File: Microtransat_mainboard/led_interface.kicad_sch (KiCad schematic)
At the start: 10 parts, among them J6 Conn_01x05

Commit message: add estop stuff kinda
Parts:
- removed J6: Conn_01x05, symbol Connector_Generic:Conn_01x05
- added J3: Conn_01x06, symbol Connector_Generic:Conn_01x06
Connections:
- net GND: now also J3.6 (Pin_6)
- net blueOut: now also J3.4 (Pin_4)
- net greenOut: now also J3.3 (Pin_3)
- net redOut: now also J3.1 (Pin_1)
- net yellowOut: now also J3.2 (Pin_2)
- net eStopOut: now reaches Logic_Shifter1.11 (B5)
- net eStopOut: now also J3.5 (Pin_5)
- net eStopTrigger: now reaches Logic_Shifter1.6 (A5)
- no-connect marks 4 -> 2
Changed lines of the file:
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@@
-	)
-	(no_connect
-		(at 165.1 87.63)
 	)
 	(no_connect
@@
 	)
 	(no_connect
-		(at 165.1 77.47)
-	)
-	(no_connect
 		(at 165.1 80.01)
 	)
@@
 			)
 			(justify right bottom)
+		)
+	)
+	(label "eStopOut"
+		(at 194.31 88.9 180)
+		(effects
+			(font
+				(size 1.27 1.27)
+			)
+			(justify right bottom)
+		)
+	)
+	(label "eStopOut"
+		(at 165.1 87.63 0)
+		(effects
+			(font
+				(size 1.27 1.27)
+			)
+			(justify left bottom)
 		)
 	)
@@
 			)
 			(justify right)
+		)
+	)
+	(hierarchical_label "eStopTrigger"
+		(shape input)
+		(at 165.1 77.47 0)
+		(effects
+			(font
+				(size 1.27 1.27)
+			)
+			(justify left)
 		)
 	)
@@
 	)
 	(symbol
-		(lib_id "Connector_Generic:Conn_01x05")
-		(at 199.39 83.82 0)
-		(unit 1)
-		(exclude_from_sim no)
-		(in_bom yes)
-		(on_board yes)
-		(dnp no)
-		(fields_autoplaced yes)
-		(property "Reference" "J6"
-			(at 201.93 82.5499 0)
-			(effects
-				(font
-					(size 1.27 1.27)
-				)
-				(justify left)
-			)
-		)
-		(property "Value" "Conn_01x05"
-			(at 201.93 85.0899 0)
-			(effects
-				(font
-					(size 1.27 1.27)
-				)
-				(justify left)
-			)
-		)
-		(property "Footprint" ""
-			(at 199.39 83.82 0)
-			(effects
-				(font
-					(size 1.27 1.27)
-				)
-				(hide yes)
-			)
-		)
-		(property "Datasheet" "~"
-			(at 199.39 83.82 0)
-			(effects
-				(font
-					(size 1.27 1.27)
-				)
-				(hide yes)
-			)
-		)
-		(property "Description" "Generic connector, single row, 01x05, script generated (kicad-library-utils/schlib/autogen/connector/)"
-			(at 199.39 83.82 0)
-			(effects
-				(font
-					(size 1.27 1.27)
-				)
-				(hide yes)
-			)
-		)
-		(pin "1"
-		)
-		(pin "2"
-		)
-		(pin "3"
-		)
-		(pin "5"
-		)
-		(pin "4"
-		)
-		(instances
-			(project "Microtransat_mainboard"
-				(path "/89914625-be83-416e-bb0d-b792f59b4aa6/2a723dab-0fe3-42a5-a32e-d625b3338ba9"
-					(reference "J6")
-					(unit 1)
-				)
-			)
-		)
-	)
-	(symbol
 		(lib_id "Device:LED")
 		(at 68.58 71.12 90)
@@
 	(symbol
 		(lib_id "power:GND")
-		(at 194.31 88.9 270)
+		(at 194.31 91.44 270)
 		(unit 1)
 		(exclude_from_sim no)
@@
 		(dnp no)
 		(property "Reference" "#PWR041"
-			(at 187.96 88.9 0)
+			(at 187.96 91.44 0)
 			(effects
 				(font
@@
 		)
 		(property "Value" "GND"
-			(at 189.23 88.9 90)
+			(at 189.23 91.44 90)
 			(effects
 				(font
@@
 		)
 		(property "Footprint" ""
-			(at 194.31 88.9 0)
+			(at 194.31 91.44 0)
 			(effects
 				(font
@@
 		)
 		(property "Datasheet" ""
-			(at 194.31 88.9 0)
+			(at 194.31 91.44 0)
 			(effects
 				(font
@@
 		)
 		(property "Description" "Power symbol creates a global label with name \"GND\" , ground"
-			(at 194.31 88.9 0)
+			(at 194.31 91.44 0)
 			(effects
 				(font
@@
 					(unit 1)
 				)
+			)
+		)
+	)
+	(symbol
+		(lib_id "Connector_Generic:Conn_01x06")
+		(at 199.39 83.82 0)
+		(unit 1)
+		(exclude_from_sim no)
+		(in_bom yes)
+		(on_board yes)
+		(dnp no)
+		(fields_autoplaced yes)
+		(property "Reference" "J3"
+			(at 201.93 83.8199 0)
+			(effects
+				(font
+					(size 1.27 1.27)
+				)
+				(justify left)
+			)
+		)
+		(property "Value" "Conn_01x06"
+			(at 201.93 86.3599 0)
+			(effects
+				(font
+					(size 1.27 1.27)
+				)
+				(justify left)
+			)
+		)
+		(property "Footprint" ""
+			(at 199.39 83.82 0)
+			(effects
+				(font
+					(size 1.27 1.27)
+				)
+				(hide yes)
+			)
+		)
+		(property "Datasheet" "~"
+			(at 199.39 83.82 0)
+			(effects
+				(font
+					(size 1.27 1.27)
+				)
+				(hide yes)
+			)
+		)
+		(property "Description" "Generic connector, single row, 01x06, script generated (kicad-library-utils/schlib/autogen/connector/)"
+			(at 199.39 83.82 0)
+			(effects
+				(font
+					(size 1.27 1.27)
+				)
+				(hide yes)
+			)
+		)
+		(pin "4"
+		)
+		(pin "1"
+		)
+		(pin "5"
+		)
+		(pin "3"
+		)
+		(pin "6"
+		)
+		(pin "2"
+		)
+		(instances
+			(project ""
+				(path "/89914625-be83-416e-bb0d-b792f59b4aa6/2a723dab-0fe3-42a5-a32e-d625b3338ba9"
+					(reference "J3")
+					(unit 1)
+				)

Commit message: puh
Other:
- note added: "Relay Out"
- note removed: "Light Tower Out"
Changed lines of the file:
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@@
 	(generator_version "9.0")
 	(paper "A4")
-	(text "Light Tower Out\n"
+	(text "Relay Out"
 		(exclude_from_sim no)
 		(at 198.882 74.93 0)

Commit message: Fixed ERC errors
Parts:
- J3: footprint (none) -> Connector_PinHeader_2.54mm:PinHeader_1x06_P2.54mm_Vertical
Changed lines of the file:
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@@
 			)
 		)
-		(property "Footprint" ""
+		(property "Footprint" "Connector_PinHeader_2.54mm:PinHeader_1x06_P2.54mm_Vertical"
 			(at 199.39 83.82 0)
 			(effects

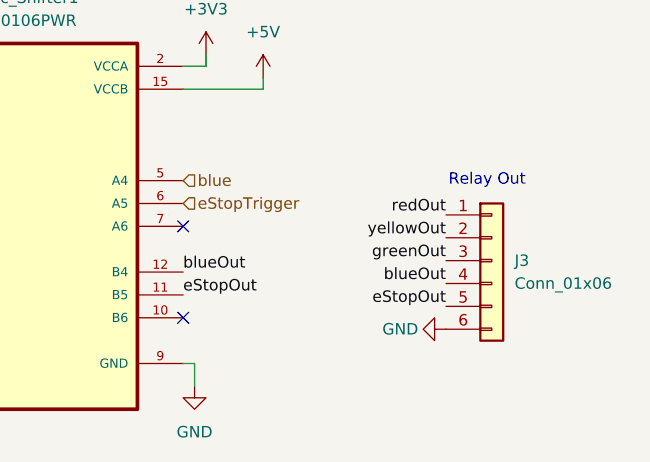
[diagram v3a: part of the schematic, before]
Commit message: Added second RC switch for mode pin, added additional relay output, changed IMU to I2C
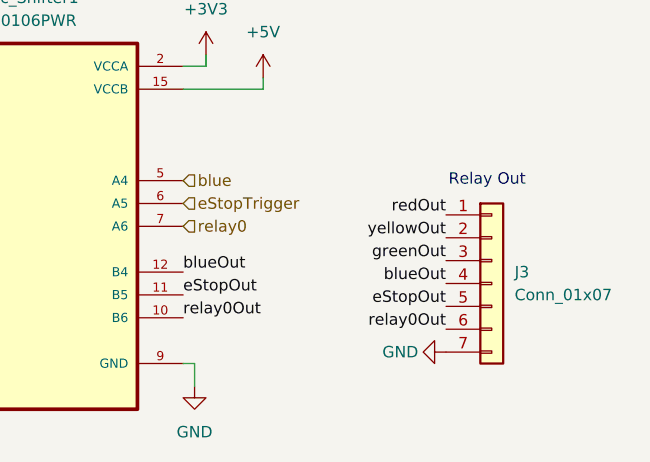
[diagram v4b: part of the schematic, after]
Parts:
- removed J3: Conn_01x06, Connector_PinHeader_2.54mm:PinHeader_1x06_P2.54mm_Vertical, symbol Connector_Generic:Conn_01x06
- added J3: Conn_01x07, Connector_PinSocket_2.54mm:PinSocket_1x07_P2.54mm_Vertical, symbol Connector_Generic:Conn_01x07
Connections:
- net GND: now also J3.7 (Pin_7)
- net blueOut: now also J3.4 (Pin_4)
- net eStopOut: now also J3.5 (Pin_5)
- net greenOut: now also J3.3 (Pin_3)
- net redOut: now also J3.1 (Pin_1)
- net yellowOut: now also J3.2 (Pin_2)
- net relay0Out: now reaches Logic_Shifter1.10 (B6)
- net relay0Out: now also J3.6 (Pin_6)
- net relay0: now reaches Logic_Shifter1.7 (A6)
- no-connect marks 2 -> 0
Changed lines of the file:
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@@
 		(color 0 0 0 0)
-	)
-	(no_connect
-		(at 165.1 90.17)
-	)
-	(no_connect
-		(at 165.1 80.01)
 	)
 	(wire
@@
 		)
 	)
+	(label "relay0Out"
+		(at 194.31 91.44 180)
+		(effects
+			(font
+				(size 1.27 1.27)
+			)
+			(justify right bottom)
+		)
+	)
 	(label "yellowOut"
 		(at 194.31 81.28 180)
@@
 			)
 			(justify right bottom)
+		)
+	)
+	(label "relay0Out"
+		(at 165.1 90.17 0)
+		(effects
+			(font
+				(size 1.27 1.27)
+			)
+			(justify left bottom)
 		)
 	)
@@
 		(shape input)
 		(at 68.58 64.77 90)
+		(effects
+			(font
+				(size 1.27 1.27)
+			)
+			(justify left)
+		)
+	)
+	(hierarchical_label "relay0"
+		(shape input)
+		(at 165.1 80.01 0)
 		(effects
 			(font
@@
 	)
 	(symbol
+		(lib_id "Connector_Generic:Conn_01x07")
+		(at 199.39 86.36 0)
+		(unit 1)
+		(exclude_from_sim no)
+		(in_bom yes)
+		(on_board yes)
+		(dnp no)
+		(fields_autoplaced yes)
+		(property "Reference" "J3"
+			(at 201.93 85.0899 0)
+			(effects
+				(font
+					(size 1.27 1.27)
+				)
+				(justify left)
+			)
+		)
+		(property "Value" "Conn_01x07"
+			(at 201.93 87.6299 0)
+			(effects
+				(font
+					(size 1.27 1.27)
+				)
+				(justify left)
+			)
+		)
+		(property "Footprint" "Connector_PinSocket_2.54mm:PinSocket_1x07_P2.54mm_Vertical"
+			(at 199.39 86.36 0)
+			(effects
+				(font
+					(size 1.27 1.27)
+				)
+				(hide yes)
+			)
+		)
+		(property "Datasheet" "~"
+			(at 199.39 86.36 0)
+			(effects
+				(font
+					(size 1.27 1.27)
+				)
+				(hide yes)
+			)
+		)
+		(property "Description" "Generic connector, single row, 01x07, script generated (kicad-library-utils/schlib/autogen/connector/)"
+			(at 199.39 86.36 0)
+			(effects
+				(font
+					(size 1.27 1.27)
+				)
+				(hide yes)
+			)
+		)
+		(pin "5"
+		)
+		(pin "2"
+		)
+		(pin "1"
+		)
+		(pin "3"
+		)
+		(pin "4"
+		)
+		(pin "6"
+		)
+		(pin "7"
+		)
+		(instances
+			(project ""
+				(path "/89914625-be83-416e-bb0d-b792f59b4aa6/2a723dab-0fe3-42a5-a32e-d625b3338ba9"
+					(reference "J3")
+					(unit 1)
+				)
+			)
+		)
+	)
+	(symbol
 		(lib_id "Device:LED")
 		(at 102.87 71.12 90)
@@
 	(symbol
 		(lib_id "power:GND")
-		(at 194.31 91.44 270)
+		(at 194.31 93.98 270)
 		(unit 1)
 		(exclude_from_sim no)
@@
 		(dnp no)
 		(property "Reference" "#PWR041"
-			(at 187.96 91.44 0)
+			(at 187.96 93.98 0)
 			(effects
 				(font
@@
 		)
 		(property "Value" "GND"
-			(at 189.23 91.44 90)
+			(at 189.23 93.98 90)
 			(effects
 				(font
@@
 		)
 		(property "Footprint" ""
-			(at 194.31 91.44 0)
+			(at 194.31 93.98 0)
 			(effects
 				(font
@@
 		)
 		(property "Datasheet" ""
-			(at 194.31 91.44 0)
+			(at 194.31 93.98 0)
 			(effects
 				(font
@@
 		)
 		(property "Description" "Power symbol creates a global label with name \"GND\" , ground"
-			(at 194.31 91.44 0)
+			(at 194.31 93.98 0)
 			(effects
 				(font
@@
 					(unit 1)
 				)
-			)
-		)
-	)
-	(symbol
-		(lib_id "Connector_Generic:Conn_01x06")
-		(at 199.39 83.82 0)
-		(unit 1)
-		(exclude_from_sim no)
-		(in_bom yes)
-		(on_board yes)
-		(dnp no)
-		(fields_autoplaced yes)
-		(property "Reference" "J3"
-			(at 201.93 83.8199 0)
-			(effects
-				(font
-					(size 1.27 1.27)
-				)
-				(justify left)
-			)
-		)
-		(property "Value" "Conn_01x06"
-			(at 201.93 86.3599 0)
-			(effects
-				(font
-					(size 1.27 1.27)
-				)
-				(justify left)
-			)
-		)
-		(property "Footprint" "Connector_PinHeader_2.54mm:PinHeader_1x06_P2.54mm_Vertical"
-			(at 199.39 83.82 0)
-			(effects
-				(font
-					(size 1.27 1.27)
-				)
-				(hide yes)
-			)
-		)
-		(property "Datasheet" "~"
-			(at 199.39 83.82 0)
-			(effects
-				(font
-					(size 1.27 1.27)
-				)
-				(hide yes)
-			)
-		)
-		(property "Description" "Generic connector, single row, 01x06, script generated (kicad-library-utils/schlib/autogen/connector/)"
-			(at 199.39 83.82 0)
-			(effects
-				(font
-					(size 1.27 1.27)
-				)
-				(hide yes)
-			)
-		)
-		(pin "4"
-		)
-		(pin "1"
-		)
-		(pin "5"
-		)
-		(pin "3"
-		)
-		(pin "6"
-		)
-		(pin "2"
-		)
-		(instances
-			(project ""
-				(path "/89914625-be83-416e-bb0d-b792f59b4aa6/2a723dab-0fe3-42a5-a32e-d625b3338ba9"
-					(reference "J3")
-					(unit 1)
-				)

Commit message: routed the traces (maybe?)
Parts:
- added C2, C3: 0.1u, Capacitor_SMD:C_1206_3216Metric_Pad1.33x1.80mm_HandSolder, symbol Device:C
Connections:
- net +3V3: now also C2.1
- net +5V: now also C3.1
- net GND: now also C2.2, C3.2

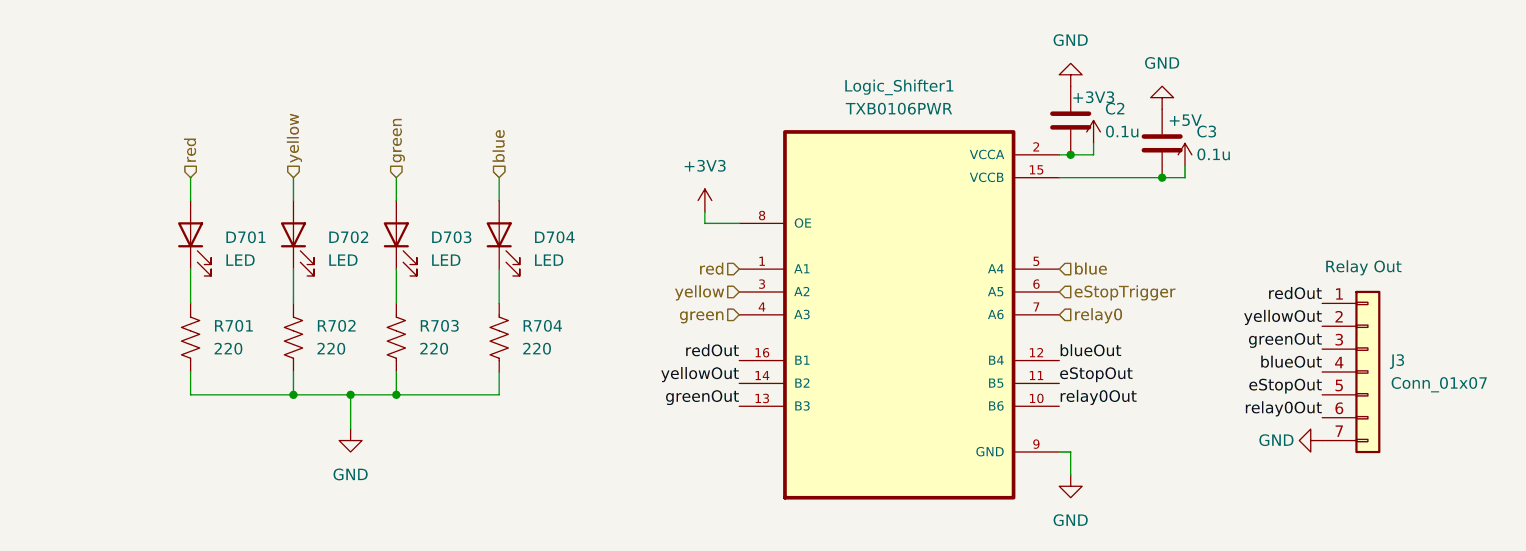
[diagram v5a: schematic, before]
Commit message: Finished silkscreen/outline changes
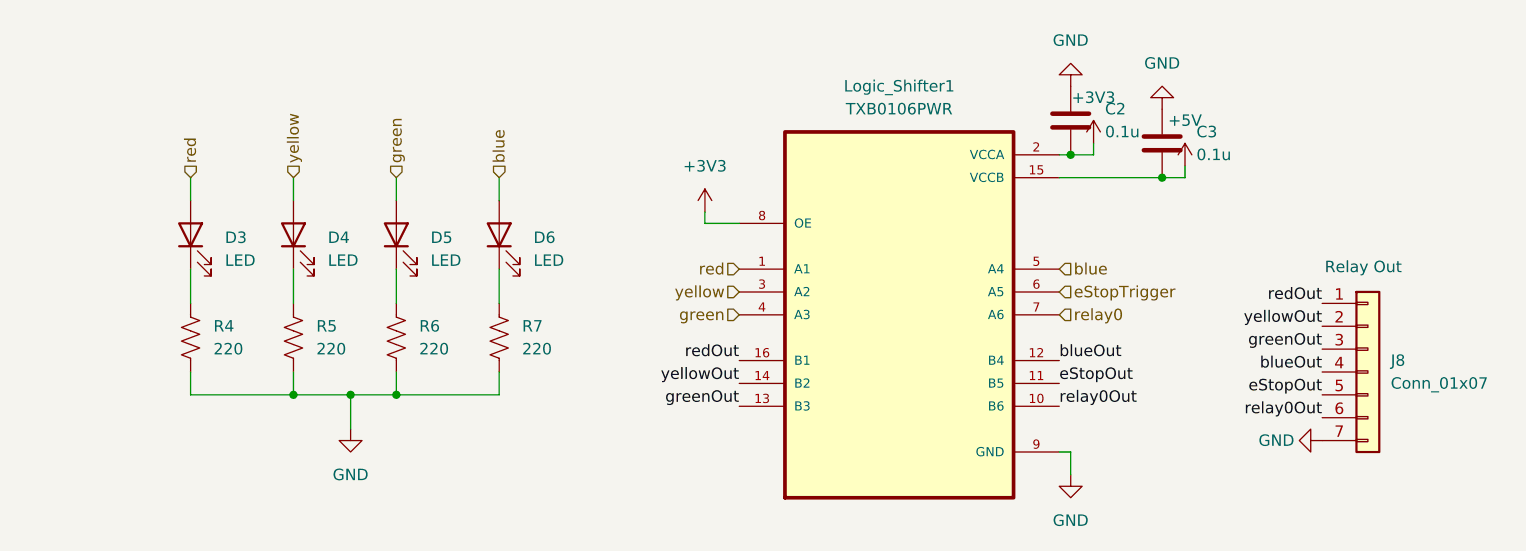
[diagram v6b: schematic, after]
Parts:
- renumbered D701 to D3, D702 to D4, D703 to D5, D704 to D6, J3 to J8, R701 to R4, R702 to R5, R703 to R6, R704 to R7
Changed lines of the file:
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@@
 		(dnp no)
 		(fields_autoplaced yes)
-		(property "Reference" "R703"
+		(property "Reference" "R6"
 			(at 93.98 81.2799 0)
 			(effects
@@
 			(project "Microtransat_mainboard"
 				(path "/89914625-be83-416e-bb0d-b792f59b4aa6/2a723dab-0fe3-42a5-a32e-d625b3338ba9"
-					(reference "R703")
+					(reference "R6")
 					(unit 1)
 				)
@@
 		(dnp no)
 		(fields_autoplaced yes)
-		(property "Reference" "R701"
+		(property "Reference" "R4"
 			(at 71.12 81.2799 0)
 			(effects
@@
 			(project "Microtransat_mainboard"
 				(path "/89914625-be83-416e-bb0d-b792f59b4aa6/2a723dab-0fe3-42a5-a32e-d625b3338ba9"
-					(reference "R701")
+					(reference "R4")
 					(unit 1)
 				)
@@
 		(dnp no)
 		(fields_autoplaced yes)
-		(property "Reference" "#PWR020"
+		(property "Reference" "#PWR031"
 			(at 168.91 64.77 0)
 			(effects
@@
 			(project "Microtransat_mainboard"
 				(path "/89914625-be83-416e-bb0d-b792f59b4aa6/2a723dab-0fe3-42a5-a32e-d625b3338ba9"
-					(reference "#PWR020")
+					(reference "#PWR031")
 					(unit 1)
 				)
@@
 		(dnp no)
 		(fields_autoplaced yes)
-		(property "Reference" "R704"
+		(property "Reference" "R7"
 			(at 105.41 81.2799 0)
 			(effects
@@
 			(project "Microtransat_mainboard"
 				(path "/89914625-be83-416e-bb0d-b792f59b4aa6/2a723dab-0fe3-42a5-a32e-d625b3338ba9"
-					(reference "R704")
+					(reference "R7")
 					(unit 1)
 				)
@@
 		(dnp no)
 		(fields_autoplaced yes)
-		(property "Reference" "D702"
+		(property "Reference" "D4"
 			(at 83.82 71.4374 90)
 			(effects
@@
 			(project "Microtransat_mainboard"
 				(path "/89914625-be83-416e-bb0d-b792f59b4aa6/2a723dab-0fe3-42a5-a32e-d625b3338ba9"
-					(reference "D702")
+					(reference "D4")
 					(unit 1)
 				)
@@
 		(dnp no)
 		(fields_autoplaced yes)
-		(property "Reference" "#PWR021"
+		(property "Reference" "#PWR033"
 			(at 179.07 67.31 0)
 			(effects
@@
 			(project "Microtransat_mainboard"
 				(path "/89914625-be83-416e-bb0d-b792f59b4aa6/2a723dab-0fe3-42a5-a32e-d625b3338ba9"
-					(reference "#PWR021")
+					(reference "#PWR033")
 					(unit 1)
 				)
@@
 		(dnp no)
 		(fields_autoplaced yes)
-		(property "Reference" "J3"
+		(property "Reference" "J8"
 			(at 201.93 85.0899 0)
 			(effects
@@
 			(project ""
 				(path "/89914625-be83-416e-bb0d-b792f59b4aa6/2a723dab-0fe3-42a5-a32e-d625b3338ba9"
-					(reference "J3")
+					(reference "J8")
 					(unit 1)
 				)
@@
 		(dnp no)
 		(fields_autoplaced yes)
-		(property "Reference" "D704"
+		(property "Reference" "D6"
 			(at 106.68 71.4374 90)
 			(effects
@@
 			(project "Microtransat_mainboard"
 				(path "/89914625-be83-416e-bb0d-b792f59b4aa6/2a723dab-0fe3-42a5-a32e-d625b3338ba9"
-					(reference "D704")
+					(reference "D6")
 					(unit 1)
 				)
@@
 		(dnp no)
 		(fields_autoplaced yes)
-		(property "Reference" "#PWR037"
+		(property "Reference" "#PWR029"
 			(at 166.37 48.26 0)
 			(effects
@@
 			(project "Microtransat_mainboard"
 				(path "/89914625-be83-416e-bb0d-b792f59b4aa6/2a723dab-0fe3-42a5-a32e-d625b3338ba9"
-					(reference "#PWR037")
+					(reference "#PWR029")
 					(unit 1)
 				)
@@
 		(dnp no)
 		(fields_autoplaced yes)
-		(property "Reference" "#PWR023"
+		(property "Reference" "#PWR030"
 			(at 166.37 104.14 0)
 			(effects
@@
 			(project "Microtransat_mainboard"
 				(path "/89914625-be83-416e-bb0d-b792f59b4aa6/2a723dab-0fe3-42a5-a32e-d625b3338ba9"
-					(reference "#PWR023")
+					(reference "#PWR030")
 					(unit 1)
 				)
@@
 		(dnp no)
 		(fields_autoplaced yes)
-		(property "Reference" "#PWR039"
+		(property "Reference" "#PWR032"
 			(at 176.53 50.8 0)
 			(effects
@@
 			(project "Microtransat_mainboard"
 				(path "/89914625-be83-416e-bb0d-b792f59b4aa6/2a723dab-0fe3-42a5-a32e-d625b3338ba9"
-					(reference "#PWR039")
+					(reference "#PWR032")
 					(unit 1)
 				)
@@
 		(dnp no)
 		(fields_autoplaced yes)
-		(property "Reference" "D703"
+		(property "Reference" "D5"
 			(at 95.25 71.4374 90)
 			(effects
@@
 			(project "Microtransat_mainboard"
 				(path "/89914625-be83-416e-bb0d-b792f59b4aa6/2a723dab-0fe3-42a5-a32e-d625b3338ba9"
-					(reference "D703")
+					(reference "D5")
 					(unit 1)
 				)
@@
 		(dnp no)
 		(fields_autoplaced yes)
-		(property "Reference" "D701"
+		(property "Reference" "D3"
 			(at 72.39 71.4374 90)
 			(effects
@@
 			(project "Microtransat_mainboard"
 				(path "/89914625-be83-416e-bb0d-b792f59b4aa6/2a723dab-0fe3-42a5-a32e-d625b3338ba9"
-					(reference "D701")
+					(reference "D3")
 					(unit 1)
 				)
@@
 		(dnp no)
 		(fields_autoplaced yes)
-		(property "Reference" "#PWR0701"
+		(property "Reference" "#PWR027"
 			(at 86.36 99.06 0)
 			(effects
@@
 			(project "Microtransat_mainboard"
 				(path "/89914625-be83-416e-bb0d-b792f59b4aa6/2a723dab-0fe3-42a5-a32e-d625b3338ba9"
-					(reference "#PWR0701")
+					(reference "#PWR027")
 					(unit 1)
 				)
@@
 		(dnp no)
 		(fields_autoplaced yes)
-		(property "Reference" "#PWR022"
+		(property "Reference" "#PWR028"
 			(at 125.73 72.39 0)
 			(effects
@@
 			(project "Microtransat_mainboard"
 				(path "/89914625-be83-416e-bb0d-b792f59b4aa6/2a723dab-0fe3-42a5-a32e-d625b3338ba9"
-					(reference "#PWR022")
+					(reference "#PWR028")
 					(unit 1)
 				)
@@
 		(on_board yes)
 		(dnp no)
-		(property "Reference" "#PWR041"
+		(property "Reference" "#PWR034"
 			(at 187.96 93.98 0)
 			(effects
@@
 			(project "Microtransat_mainboard"
 				(path "/89914625-be83-416e-bb0d-b792f59b4aa6/2a723dab-0fe3-42a5-a32e-d625b3338ba9"
-					(reference "#PWR041")
+					(reference "#PWR034")
 					(unit 1)
 				)
@@
 		(dnp no)
 		(fields_autoplaced yes)
-		(property "Reference" "R702"
+		(property "Reference" "R5"
 			(at 82.55 81.2799 0)
 			(effects
@@
 			(project "Microtransat_mainboard"
 				(path "/89914625-be83-416e-bb0d-b792f59b4aa6/2a723dab-0fe3-42a5-a32e-d625b3338ba9"
-					(reference "R702")
-					(unit 1)
-				)
+					(reference "R5")
+					(unit 1)
+				)
